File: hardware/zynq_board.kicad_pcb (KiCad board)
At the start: 8 copper layers, 120 x 75 mm, 411 parts, among them J1 USB_OTG, J10 DM3CS, J11 USB_OTG, J12 Conn_01x02, J6 MDR20, J7 LSHM-150-xxx-x-DV-A-S, J9 Conn_01x02, Q1 DMP3056L, U1 xc7z030sbg485, U10 TPS3808G01, U11 MCP1700-2502E_SOT23, U12 MT41K128M8, U13 TPS51206, U14 MT41K128M8, U15 DIFF_OSC, U16 DIFF_OSC, U17 SI53340, U18 NX5P3090, U19 SMP1255PUTG, U2 SFPP_CONN, U20 USB3320, U21 OSC, U22 TLK10031, U23 SN74AXC8T245, U24 SN74AXC8T245, U25 SN74AXC8T245, U26 LSF0102, U27 LSF0102, U28 SN74LVC2T45, U29 SN74LVC2T45, U3 TPS8208x, U30 SN74LVC2T45, U31 SN74LVC2T45, U32 DMF05LCFLP, U33 DMF05LCFLP, U34 TC1262-33, U35 MAX14854, U36 CAT24C02TDI-GT3, U37 EMIF06-MSD02N16, U38 33.333MHZ, U39 SMP1255PUTG, U4 TPS8208x, U40 FT234XD, U41 SN74LV1T126, U42 SN74LV1T126, U5 TPSM84424, U6 TPSM84424, U7 TPS8208x, U8 TPS8208x, U9 TPS8208x

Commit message: Added Power/Protection Circuit
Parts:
- removed C134: 100 nF, Capacitors_SMD:C_0201
- removed C135: 0.1µF, Capacitors_SMD:C_0402
- removed F1: Fuse, Resistors_SMD:R_0402
- removed the REF** at (160.0, 64.0)
- removed the REF** at (74.0, 64.0)
- added C748: 100 nF, Capacitors_SMD:C_0201, B.Cu at (180.0, 116.4)
- added C749: 100 nF, Capacitors_SMD:C_0201, F.Cu at (157.6, 123.8)
- added D2201: P0220SCMCLRP, footprints:DO-214AA, F.Cu at (174.5, 71.5)
- added D2204: BAT54GWJ, Diodes_SMD:D_SOD-123, B.Cu at (175.0, 65.5)
- added F2201: Fuse, Fuse_Holders_and_Fuses:Fuse_SMD1206_Reflow, B.Cu at (175.0, 74.0)
- added T2201: 500 Ohm@100 MHz, footprints:DLW5BTM_5.00x5.00mm, F.Cu at (168.6, 71.5)
- D2202: renamed from D6; moved to B.Cu
- D2203: renamed from D7; moved to B.Cu
- moved D2202 200.9 mm to (175.0, 69.5)
- moved D2203 77.1 mm to (167.7, 70.2), turned to 270 degrees
- moved Q2201 67.2 mm to (162.0, 73.8)
- moved REF** 26.0 mm to (74.0, 64.0)
- moved J1601 10.3 mm to (130.2, 129.2)
- moved C711 7.69 mm to (176.0, 100.7)
- moved C708 7.62 mm to (180.8, 93.2)
- moved C746 7.62 mm to (172.8, 116.4)
- moved C756 7.62 mm to (179.8, 94.7)
- moved C761 7.62 mm to (150.8, 107.2)
- moved C705 7.62 mm to (182.4, 93.2)
- moved C716 7.62 mm to (176.0, 93.2)
- moved C718 7.62 mm to (173.2, 100.9)
- moved C721 7.62 mm to (174.4, 93.2)
- moved C724 7.62 mm to (170.7, 101.4)
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- renumbered C153 to C1001, C154 to C1002, C155 to C1003, C156 to C1004, C157 to C1201, C158 to C1202, C159 to C1203, C160 to C1204, C161 to C1205, C162 to C1206, C163 to C1207, C164 to C1208, C165 to C1209, C166 to C1210, C167 to C1211, C168 to C1212, C169 to C1213, C170 to C1214, C171 to C1215, C172 to C1216, C173 to C1217, C174 to C1218, C175 to C1219, C176 to C1220, C177 to C1221, C178 to C1222, C179 to C1223, C180 to C1224, C181 to C1225, C182 to C1226, C183 to C1227, C184 to C1228, C185 to C1229, C186 to C1230, C187 to C1231, C188 to C1232, C189 to C1233, C190 to C1234, C191 to C1235, C192 to C1236, C193 to C1237, C194 to C1238, C195 to C1301, C196 to C1302, C197 to C1303, C198 to C1304, C199 to C1305, C200 to C1306, C201 to C1307, C202 to C1308, C203 to C1309, C204 to C1310, C205 to C1311, C206 to C1312, C207 to C1313, C208 to C1314, C209 to C1315, C210 to C1316, C211 to C1317, C212 to C1318, C213 to C1319, C214 to C1320, C215 to C1401, C216 to C1402, C217 to C1403, C218 to C1404, C219 to C1405, C220 to C1406, C221 to C1407, C222 to C1408, C231 to C1509, C232 to C1510, C239 to C1801, C240 to C1802, C241 to C1803, C243 to C1901, C244 to C1902, C245 to C1903, C246 to C1904, C247 to C1905, C248 to C1906, C249 to C1907, C250 to C1908, C251 to C1909, C1 to C201, C3 to C203, C4 to C204, C5 to C205, C6 to C206, C7 to C207, C8 to C208, C9 to C209, C10 to C210, C11 to C211, C12 to C212, C13 to C213, C14 to C214, C15 to C215, C16 to C216, C17 to C217, C18 to C218, C19 to C219, C20 to C220, C21 to C221, C22 to C222, C23 to C223, C24 to C224, C25 to C225, C26 to C226, C27 to C227, C28 to C228, C29 to C229, C30 to C230, C31 to C231, C32 to C232, C33 to C233, C34 to C234, C35 to C235, C36 to C236, C37 to C237, C38 to C238, C39 to C239, C40 to C240, C41 to C241, C42 to C242, C43 to C243, C44 to C244, C45 to C245, C46 to C246, C47 to C247, C48 to C248, C49 to C249, C50 to C250, C51 to C251, C52 to C252, C53 to C253, C54 to C254, C55 to C255, C56 to C256, C57 to C257, C58 to C258, C59 to C501, C60 to C502, C61 to C503, C62 to C504, C63 to C505, C64 to C506, C85 to C621, C86 to C622, C87 to C701, C88 to C702, C89 to C703, C90 to C704, C91 to C705, C92 to C706, C93 to C707, C94 to C708, C95 to C709, C96 to C710, C97 to C711, C98 to C712, C99 to C713, C100 to C714, C101 to C715, C102 to C716, C103 to C717, C104 to C718, C105 to C719, C106 to C720, C107 to C721, C108 to C722, C109 to C723, C110 to C724, C111 to C725, C112 to C726, C113 to C727, C114 to C728, C115 to C729, C116 to C730, C117 to C731, C118 to C732, C119 to C733, C120 to C734, C121 to C735, C122 to C736, C123 to C737, C124 to C738, C125 to C739, C126 to C740, C127 to C741, C128 to C742, C129 to C743, C130 to C744, C131 to C745, C132 to C746, C133 to C747, C136 to C750, C137 to C751, C252 to C752, C253 to C753, C254 to C754, C255 to C755, C138 to C756, C256 to C757, C257 to C758, C258 to C759, C259 to C760, C139 to C761, C140 to C762, C141 to C801, C142 to C802, C143 to C803, C144 to C804, C145 to C805, C146 to C901, C147 to C902, C148 to C903, C149 to C904, C150 to C905, C151 to C906, C152 to C907, D1 to D1401, D2 to D1402, D4 to D1701, J6 to J1501, J7 to J1601, J9 to J1702, J10 to J1801, J11 to J1901, J12 to J2201, J1 to J901, L5 to L1901, L1 to L201, Q1 to Q2201, R78 to R1101, R79 to R1102, R80 to R1201, R81 to R1202, R82 to R1203, R83 to R1204, R84 to R1205, R85 to R1206, R86 to R1301, R87 to R1302, R88 to R1303, R89 to R1304, R90 to R1305, R91 to R1306, R92 to R1307, R93 to R1308, R94 to R1309, R95 to R1310, R96 to R1311, R97 to R1312, R98 to R1313, R99 to R1314, R100 to R1315, R101 to R1316, R102 to R1317, R103 to R1318, R104 to R1319, R105 to R1320, R106 to R1401, R107 to R1402, R108 to R1403, R109 to R1404, R110 to R1405, R111 to R1406, R112 to R1407, R113 to R1408, R114 to R1409, R115 to R1410, R116 to R1411, R117 to R1412, R118 to R1413, R119 to R1414, R120 to R1415, R121 to R1416, R122 to R1417, R123 to R1418, R124 to R1419, R125 to R1420, R126 to R1421, R142 to R1701, R143 to R1702, R144 to R1801, R145 to R1802, R146 to R1803, R147 to R1804, R148 to R1805, R149 to R1806, R150 to R1807, R151 to R1808, R152 to R1809, R153 to R1810, R154 to R1811, R155 to R1812, R156 to R1813, R157 to R1814, R158 to R1815, R159 to R1816, R161 to R1901, R162 to R1902, R163 to R1903, R164 to R1904, R165 to R1905, R1 to R501, R2 to R502, R3 to R503, R4 to R504, R5 to R505, R6 to R506, R7 to R507, R8 to R508, R9 to R509, R10 to R510, R11 to R511, R39 to R701, R40 to R702, R41 to R703, R42 to R704, R43 to R705, R44 to R706, R45 to R707, R46 to R708, R47 to R709, R48 to R710, R49 to R711, R50 to R712, R51 to R713, R166 to R714, R53 to R715, R52 to R716, R54 to R717, R55 to R718, R56 to R719, R57 to R720, R58 to R721, R59 to R722, R60 to R723, R61 to R724, R62 to R725, R63 to R726, R64 to R727, R65 to R728, R167 to R729, R168 to R730, R66 to R731, R67 to R732, R68 to R801, R69 to R802, R70 to R803, R71 to R804, R72 to R901, R73 to R902, R74 to R903, R75 to R904, R76 to R905, U22 to U1201, U23 to U1401, U24 to U1402, U25 to U1403, U26 to U1404, U27 to U1405, U28 to U1501, U29 to U1502, U30 to U1503, U31 to U1504, U32 to U1505, U33 to U1506, U34 to U1507, U35 to U1508, U36 to U1801, U37 to U1802, U38 to U1803, U39 to U1901, U40 to U1902, U41 to U1903, U42 to U1904, U1 to U201, U2 to U501, U3 to U601, U4 to U602, U5 to U603, U6 to U604, U7 to U605, U8 to U606, U9 to U607, U10 to U608, U11 to U609, U12 to U701, U13 to U702, U14 to U703, U15 to U801, U16 to U802, U17 to U803, U18 to U901, U19 to U902, U20 to U903, U21 to U904
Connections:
- D2202 pad 2: Net-(D6-Pad2) -> Net-(D2202-Pad2)
- D2203 pad 3: Net-(D6-Pad2) -> Net-(D2203-Pad3)
- U701 pad E3: /DDR/DQ6 -> /DDR/DQ5
- U701 pad F2: /DDR/DQ7 -> /DDR/DQ6
- U701 pad G2: /DDR/DQ5 -> /DDR/DQ7
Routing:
- net Net-(D2202-Pad1): track 0.00 -> 27.0 mm, vias 0 -> 9
- net /DDR/DQ10: track 37.7 -> 17.2 mm
- net /DDR/DQ12: track 41.7 -> 22.0 mm
- net /DDR/DQ11: track 37.4 -> 18.7 mm
- net /DDR/DQ13: track 40.6 -> 22.5 mm
- net GND: track 144.7 -> 162.7 mm, vias 175 -> 184
- net /DDR/DQ14: track 38.9 -> 24.1 mm
- net /DDR/DQ15: track 38.5 -> 25.1 mm
- net /DDR/DDR_DQS1_P: track 39.8 -> 26.9 mm
- net /DDR/DDR_DQS1_N: track 39.1 -> 26.3 mm
- net /DDR/DQ9: track 40.7 -> 31.3 mm
- net Net-(D2201-Pad1): track 0.00 -> 7.22 mm, vias 0 -> 5
- net /DDR/DQ8: track 40.7 -> 33.9 mm
- net /DDR/DDR_DM1: track 40.6 -> 44.8 mm
- net Net-(D2202-Pad2): track 0.00 -> 4.00 mm
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- added copper zone on B.Cu, net Net-(D2201-Pad1)
- added copper zone on F.Cu, net Net-(D2201-Pad1)
- added copper zone on F.Cu, net Net-(D2201-Pad2)
- added copper zone on B.Cu, net Net-(D2202-Pad1)
- added copper zone on F.Cu, net Net-(D2202-Pad1)
- added copper zone on B.Cu, net Net-(F2201-Pad2)

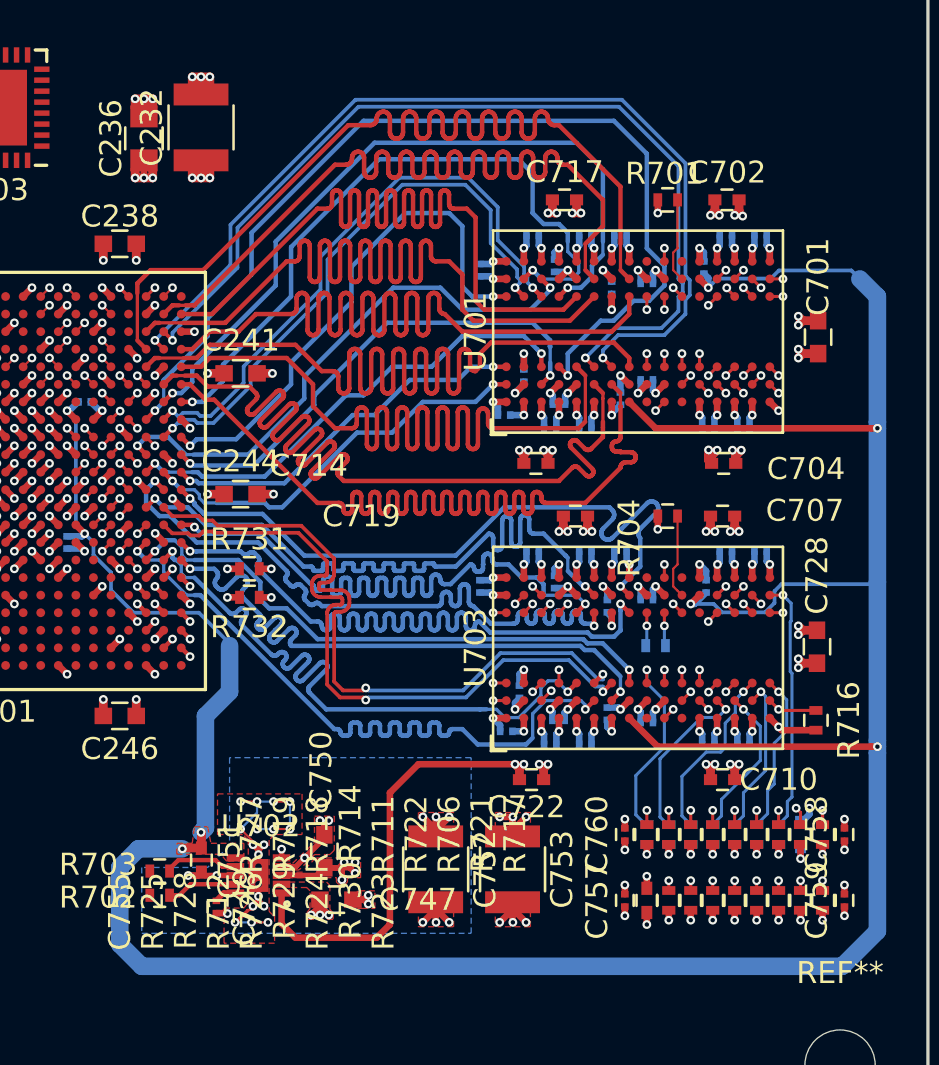
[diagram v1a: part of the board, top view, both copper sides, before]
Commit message: Length matched DDR3 Memory again.
Forgot to keep enough space between the traces and between the meander waves.

Also, I switched to Kicad 5.0 RC2.

Swaped a few ddr signals.
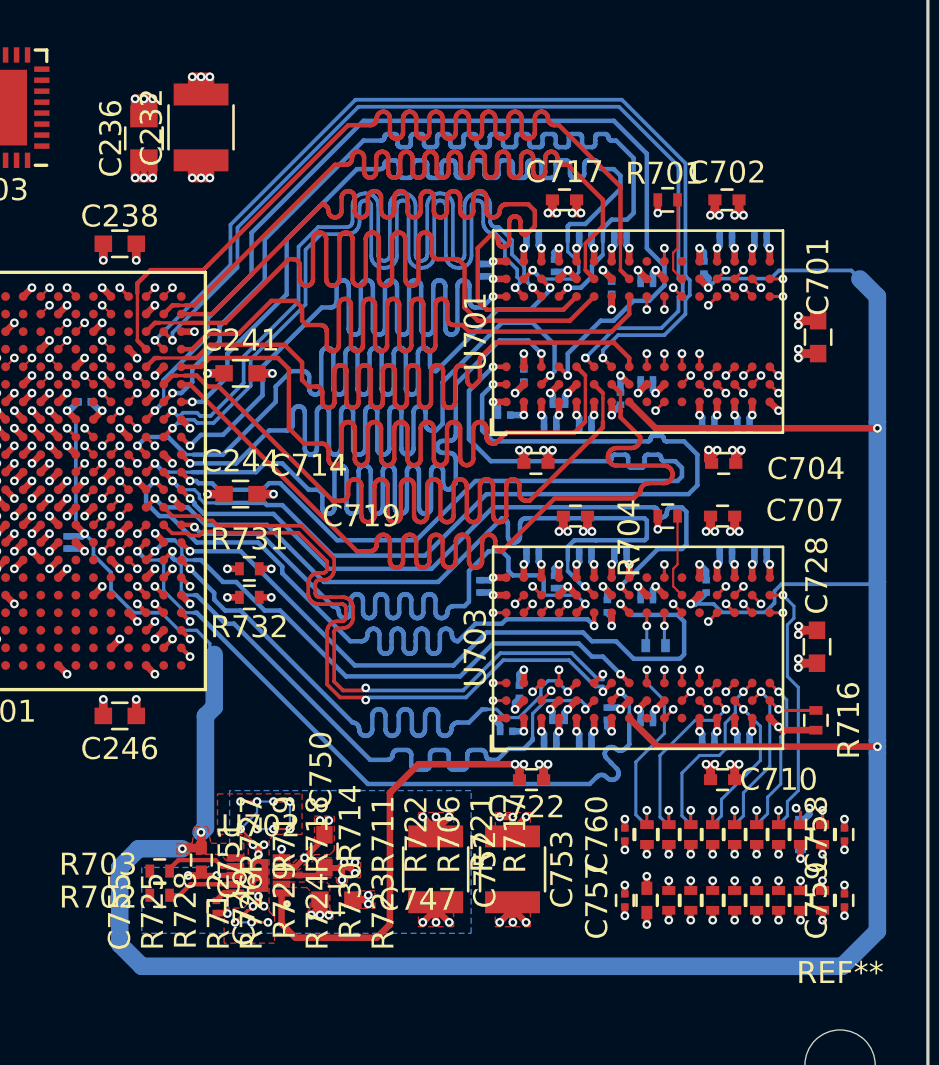
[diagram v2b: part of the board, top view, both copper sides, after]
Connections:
- R1701 pad 1: (no net) -> Net-(R1701-Pad1)
- U1201 pad A10: (no net) -> Net-(U1201-PadA10)
- U1201 pad A9: (no net) -> Net-(U1201-PadA9)
- U1201 pad B8: (no net) -> Net-(J1303-Pad3)
- U1201 pad C11: (no net) -> Net-(U1201-PadC11)
- U1201 pad C8: (no net) -> Net-(J1303-Pad1)
- U1201 pad D4: (no net) -> Net-(U1201-PadD4)
- U1201 pad D6: (no net) -> Net-(J1303-Pad2)
- U1201 pad E5: (no net) -> Net-(J1303-Pad5)
- U1201 pad E9: (no net) -> Net-(J1301-Pad1)
- U1201 pad G12: (no net) -> Net-(U1201-PadG12)
- U1201 pad H12: (no net) -> Net-(U1201-PadH12)
- U1201 pad H9: (no net) -> Net-(U1201-PadH9)
- U1201 pad J9: (no net) -> Net-(J1302-Pad1)
- U1201 pad K12: (no net) -> Net-(U1201-PadK12)
- U1201 pad K8: (no net) -> Net-(U1201-PadK8)
- U1201 pad L12: (no net) -> Net-(U1201-PadL12)
- U1402 pad 10: (no net) -> Net-(U1402-Pad10)
- U1402 pad 14: (no net) -> Net-(U1402-Pad14)
- U1403 pad 10: (no net) -> Net-(U1403-Pad10)
- U1403 pad 14: (no net) -> Net-(U1403-Pad14)
- U1403 pad 15: (no net) -> Net-(U1403-Pad15)
- U1403 pad 9: (no net) -> Net-(U1403-Pad9)
- U1501 pad B2: (no net) -> Net-(R1508-Pad1)
- U1501 pad C2: (no net) -> Net-(R1509-Pad2)
- U1501 pad D2: (no net) -> Net-(R1501-Pad1)
- U1502 pad B2: (no net) -> Net-(R1510-Pad1)
- U1502 pad C2: (no net) -> Net-(R1511-Pad2)
- U1502 pad D2: (no net) -> Net-(R1503-Pad1)
- U1503 pad B2: (no net) -> Net-(R1512-Pad1)
- U1503 pad C2: (no net) -> Net-(R1513-Pad2)
- U1503 pad D2: (no net) -> Net-(R1505-Pad1)
- U1504 pad A2: (no net) -> Net-(U1504-PadA2)
- U1504 pad B2: (no net) -> Net-(R1514-Pad1)
- U1504 pad C2: (no net) -> Net-(R1515-Pad2)
- U1504 pad D2: (no net) -> Net-(10k1501-Pad1)
- U1505 pad 6: (no net) -> Net-(U1505-Pad6)
- U1506 pad 6: (no net) -> Net-(U1506-Pad6)
- U1508 pad 16: (no net) -> Net-(C1513-Pad1)
- U1802 pad 2: (no net) -> Net-(U1802-Pad2)
- U1902 pad 11: (no net) -> Net-(U1902-Pad11)
- U1902 pad 6: (no net) -> Net-(U1902-Pad6)
- U1902 pad 8: (no net) -> Net-(U1902-Pad8)
- U201 pad A10: (no net) -> Net-(U201-PadA10)
- U201 pad A15: (no net) -> Net-(U201-PadA15)
- U201 pad A17: (no net) -> Net-(U201-PadA17)
- U201 pad A22: (no net) -> Net-(U201-PadA22)
- U201 pad B13: (no net) -> Net-(U201-PadB13)
- U201 pad B16: (no net) -> Net-(U201-PadB16)
- U201 pad B17: (no net) -> Net-(U201-PadB17)
- U201 pad B19: (no net) -> Net-(U201-PadB19)
- U201 pad C11: (no net) -> Net-(U201-PadC11)
- U201 pad C13: (no net) -> Net-(U201-PadC13)
- U201 pad C14: (no net) -> /Processing System IO/PS_RESET
- U201 pad C18: (no net) -> Net-(U201-PadC18)
- U201 pad C19: (no net) -> Net-(U201-PadC19)
- U201 pad C4: (no net) -> /GPIO_5
- U201 pad C5: (no net) -> /GPIO_4
- U201 pad C6: (no net) -> /GPIO_3
- U201 pad C8: (no net) -> /GPIO_0
- U201 pad C9: (no net) -> Net-(U201-PadC9)
- U201 pad D10: (no net) -> Net-(U201-PadD10)
- U201 pad D12: (no net) -> Net-(U201-PadD12)
- U201 pad D13: (no net) -> Net-(U201-PadD13)
- U201 pad D16: (no net) -> Net-(U201-PadD16)
- U201 pad D17: (no net) -> Net-(U201-PadD17)
- U201 pad D7: (no net) -> /GPIO_2
- U201 pad D8: (no net) -> /GPIO_1
- U201 pad E14: (no net) -> Net-(U201-PadE14)
- U201 pad E17: (no net) -> Net-(U201-PadE17)
- U201 pad E4: (no net) -> /GPIO_7
- U201 pad E5: (no net) -> /GPIO_6
- U201 pad F11: (no net) -> Net-(U201-PadF11)
- U201 pad F12: (no net) -> Net-(U201-PadF12)
- U201 pad F15: (no net) -> Net-(U201-PadF15)
- U201 pad F5: (no net) -> Net-(U201-PadF5)
- U201 pad F6: (no net) -> Net-(U201-PadF6)
- U201 pad F7: (no net) -> Net-(U201-PadF7)
- U201 pad G16: (no net) -> Net-(U201-PadG16)
- U201 pad G17: (no net) -> Net-(U201-PadG17)
- U201 pad G4: (no net) -> /GPIO_8
- U201 pad G6: (no net) -> Net-(U201-PadG6)
- U201 pad G7: (no net) -> Net-(U201-PadG7)
- U201 pad G8: (no net) -> Net-(U201-PadG8)
- U201 pad G9: (no net) -> Net-(J1101-Pad3)
- U201 pad H10: (no net) -> Net-(J1101-Pad4)
- U201 pad H11: (no net) -> Net-(J1101-Pad1)
- U201 pad H3: (no net) -> Net-(U201-PadH3)
- U201 pad H5: (no net) -> Net-(U201-PadH5)
- U201 pad H6: (no net) -> Net-(U201-PadH6)
- U201 pad H8: (no net) -> Net-(U201-PadH8)
- U201 pad H9: (no net) -> Net-(J1101-Pad2)
- U201 pad J6: (no net) -> Net-(U201-PadJ6)
- U201 pad J7: (no net) -> Net-(U201-PadJ7)
- U201 pad J8: (no net) -> Net-(U201-PadJ8)
- U201 pad K4: (no net) -> /GPIO_9
- U201 pad K7: (no net) -> Net-(U201-PadK7)
- U201 pad K8: (no net) -> Net-(U201-PadK8)
- U201 pad L4: (no net) -> /GPIO_10
- U201 pad L6: (no net) -> Net-(U201-PadL6)
- U201 pad L7: (no net) -> Net-(U201-PadL7)
- U201 pad M4: (no net) -> /GPIO_11
- U201 pad M6: (no net) -> Net-(U201-PadM6)
- U201 pad M7: (no net) -> Net-(U201-PadM7)
- U201 pad M8: (no net) -> Net-(U201-PadM8)
- U201 pad N4: (no net) -> /GPIO_12
- U201 pad N5: (no net) -> Net-(U201-PadN5)
- U201 pad N6: (no net) -> Net-(U201-PadN6)
- U201 pad N8: (no net) -> Net-(U201-PadN8)
- U201 pad P5: (no net) -> Net-(U201-PadP5)
- U201 pad P6: (no net) -> Net-(U201-PadP6)
- U201 pad P7: (no net) -> Net-(U201-PadP7)
- U201 pad P8: (no net) -> Net-(U201-PadP8)
- U201 pad R17: (no net) -> Net-(U201-PadR17)
- U201 pad R3: (no net) -> /GPIO_14
- U201 pad R4: (no net) -> /GPIO_13
- U201 pad R5: (no net) -> Net-(U201-PadR5)
- U201 pad R7: (no net) -> Net-(U201-PadR7)
- U201 pad R8: (no net) -> Net-(U201-PadR8)
- U201 pad T10: (no net) -> Net-(U201-PadT10)
- U201 pad T16: (no net) -> Net-(U201-PadT16)
- U201 pad T17: (no net) -> Net-(U201-PadT17)
- U201 pad U13: (no net) -> Net-(U201-PadU13)
- U201 pad U14: (no net) -> Net-(U201-PadU14)
- U201 pad U16: (no net) -> Net-(U201-PadU16)
- U201 pad U2: (no net) -> /GPIO_15
- U201 pad U7: (no net) -> Net-(R1001-Pad1)
- U201 pad W3: (no net) -> Net-(L202-Pad2)
- U601 pad 7: (no net) -> Net-(R608-Pad2)
- U602 pad 7: (no net) -> Net-(R610-Pad2)
- U603 pad 10: (no net) -> Net-(U603-Pad10)
- U603 pad 15: (no net) -> GND
- U603 pad 16: (no net) -> Net-(U603-Pad16)
- U603 pad 2: (no net) -> Net-(R612-Pad2)
- U603 pad 24: (no net) -> Net-(R605-Pad1)
- U603 pad 4: (no net) -> Net-(U603-Pad4)
- U603 pad 5: (no net) -> Net-(R603-Pad1)
- U603 pad 6: (no net) -> Net-(R601-Pad2)
- U604 pad 15: (no net) -> GND
- U604 pad 16: (no net) -> Net-(U604-Pad16)
- U604 pad 2: (no net) -> Net-(R614-Pad2)
- U604 pad 24: (no net) -> Net-(R606-Pad1)
- U604 pad 4: (no net) -> Net-(U604-Pad4)
- U604 pad 5: (no net) -> Net-(R604-Pad1)
- U604 pad 6: (no net) -> Net-(R602-Pad2)
- U605 pad 7: (no net) -> Net-(R621-Pad2)
- U606 pad 7: (no net) -> Net-(R623-Pad2)
- U607 pad 7: (no net) -> Net-(R625-Pad2)
- U608 pad 1: (no net) -> Net-(C614-Pad1)
- U608 pad 3: (no net) -> Net-(U608-Pad3)
- U701 pad J1: (no net) -> Net-(U701-PadJ1)
- U701 pad J9: (no net) -> Net-(U701-PadJ9)
- U701 pad L1: (no net) -> Net-(U701-PadL1)
- U701 pad L9: (no net) -> Net-(U701-PadL9)
- U701 pad M7: (no net) -> Net-(U701-PadM7)
- U703 pad E3: /DDR/DQ21 -> /DDR/DQ19
- U703 pad F2: /DDR/DQ20 -> /DDR/DQ21
- U703 pad G2: /DDR/DQ19 -> /DDR/DQ20
- U703 pad J1: (no net) -> Net-(U703-PadJ1)
- U703 pad J9: (no net) -> Net-(U703-PadJ9)
- U703 pad L1: (no net) -> Net-(U703-PadL1)
- U703 pad L9: (no net) -> Net-(U703-PadL9)
- U703 pad M7: (no net) -> Net-(U703-PadM7)
- U801 pad 1: (no net) -> Net-(U801-Pad1)
- U801 pad 2: (no net) -> Net-(U801-Pad2)
- U802 pad 1: (no net) -> Net-(U802-Pad1)
- U802 pad 2: (no net) -> Net-(U802-Pad2)
- U803 pad 13: (no net) -> Net-(U803-Pad13)
- U803 pad 14: (no net) -> Net-(U803-Pad14)
- U803 pad 15: (no net) -> Net-(U803-Pad15)
- U803 pad 16: (no net) -> Net-(U803-Pad16)
- U803 pad 8: (no net) -> Net-(U803-Pad8)
- U903 pad 12: (no net) -> Net-(U903-Pad12)
- U903 pad 15: (no net) -> Net-(U903-Pad15)
- U903 pad 16: (no net) -> Net-(U903-Pad16)
- U903 pad 25: (no net) -> Net-(U903-Pad25)
- U903 pad 27: (no net) -> /USB/RESETB
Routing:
- net /DDR/DQ10: track 17.2 -> 41.8 mm
- net /DDR/DQ12: track 22.0 -> 45.9 mm
- net /DDR/DQ11: track 18.7 -> 42.1 mm
- net /DDR/DQ13: track 22.5 -> 44.7 mm
- net /DDR/DQ14: track 24.1 -> 43.0 mm
- net /DDR/DQ15: track 25.1 -> 42.7 mm
- net /DDR/DDR_DQS1_P: track 26.9 -> 44.0 mm
- net /DDR/DDR_DQS1_N: track 26.3 -> 43.5 mm
- net /DDR/DQ9: track 31.3 -> 44.8 mm
- net /DDR/DQ8: track 33.9 -> 44.8 mm
- net /DDR/DQ24: track 24.3 -> 28.6 mm
- net /DDR/DDR_DQS3_P: track 26.5 -> 30.9 mm
- net /DDR/DQ27: track 28.4 -> 32.7 mm
- net /DDR/DQ26: track 25.5 -> 29.8 mm
- net /DDR/DQ25: track 28.4 -> 32.7 mm
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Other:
- board text added: "DQS0 is routed on an outer Layer, but the other Signals of its Group is on an inner Layer. Check, if this is a problem."

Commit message: Layouted most of the Power Circuit and Triggerbus Levelshifters.
Added Footprint for Tantal Caps. Modified Footprint for MDR20 Connector, SD-Card.

Fixed Symbol and Circuit for Power Supervisor/Delay IC.

Also fixed some smaller things in the schematics.
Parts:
- added C1501: 100 nF, Capacitor_SMD:C_0201_0603Metric, B.Cu at (90.0, 95.8)
- added C1502: 100 nF, Capacitor_SMD:C_0201_0603Metric, B.Cu at (90.0, 91.8)
- added C1503: 100 nF, Capacitor_SMD:C_0201_0603Metric, B.Cu at (90.0, 87.8)
- added C1504: 100 nF, Capacitor_SMD:C_0201_0603Metric, B.Cu at (90.0, 83.8)
- added C1505: 100 nF, Capacitor_SMD:C_0201_0603Metric, B.Cu at (88.0, 95.8)
- added C1506: 100 nF, Capacitor_SMD:C_0201_0603Metric, B.Cu at (88.0, 91.8)
- added C1507: 100 nF, Capacitor_SMD:C_0201_0603Metric, B.Cu at (88.0, 87.8)
- added C1508: 100 nF, Capacitor_SMD:C_0201_0603Metric, B.Cu at (88.0, 83.9)
- added C1511: 1 µF 6,3 V, Capacitor_SMD:C_0402_1005Metric, F.Cu at (95.5, 69.5)
- added C1512: 100 nF, Capacitor_SMD:C_0201_0603Metric, F.Cu at (94.5, 69.5)
- added C1513: 1 µF 6,3 V, Capacitor_SMD:C_0402_1005Metric, F.Cu at (85.0, 69.5)
- added C1514: 100 nF, Capacitor_SMD:C_0201_0603Metric, F.Cu at (86.0, 69.5)
- added C1515: 100 nF, Capacitor_SMD:C_0201_0603Metric, F.Cu at (86.0, 77.0)
- added C1516: 1 µF 6,3 V, Capacitor_SMD:C_0402_1005Metric, F.Cu at (85.0, 77.0)
- added C1804: 1nF, Capacitor_SMD:C_0402_1005Metric, F.Cu at (216.1, 98.2)
- added C601: 10uF 25V, Capacitor_SMD:C_1210_3225Metric, F.Cu at (157.0, 65.8)
- added C602: 10uF 25V, Capacitor_SMD:C_1210_3225Metric, F.Cu at (141.0, 65.8)
- added C603: 10uF 25V, Capacitor_SMD:C_1210_3225Metric, F.Cu at (145.0, 65.8)
- added C604: 10uF 25V, Capacitor_SMD:C_1210_3225Metric, F.Cu at (129.0, 65.8)
- added C605: 10uF, Capacitor_SMD:C_0805_2012Metric, F.Cu at (138.5, 76.8)
- added C606: 10uF, Capacitor_SMD:C_0805_2012Metric, F.Cu at (147.0, 76.8)
- added C607: 47uF 6.3V, Capacitor_SMD:C_1210_3225Metric, F.Cu at (134.8, 78.5)
- added C608: 47uF 6.3V, Capacitor_SMD:C_1210_3225Metric, F.Cu at (143.2, 78.5)
- added C609: 47uF 6.3V, Capacitor_SMD:C_1210_3225Metric, F.Cu at (145.0, 72.0)
- added C610: 100uF 6.3V, Capacitor_SMD:C_1210_3225Metric, F.Cu at (141.0, 72.0)
- added C611: 100uF 6.3V, Capacitor_SMD:C_1210_3225Metric, F.Cu at (129.0, 72.0)
- added C612: 220uF 6.3V 15mΩ, footprints:C7343-31_KEMET-D_10.22x5.6mm, B.Cu at (157.0, 67.0)
- added C613: 220uF 6.3V 15mΩ, footprints:C7343-31_KEMET-D_10.22x5.6mm, B.Cu at (141.0, 67.0)
- added C614: 1nF, Capacitor_SMD:C_0402_1005Metric, F.Cu at (126.2, 69.2)
- added C615: 10uF, Capacitor_SMD:C_0805_2012Metric, F.Cu at (129.9, 76.8)
- added C616: 10uF, Capacitor_SMD:C_0805_2012Metric, F.Cu at (121.5, 76.8)
- added C617: 10uF, Capacitor_SMD:C_0805_2012Metric, F.Cu at (155.4, 76.8)
- added C618: 47uF 6.3V, Capacitor_SMD:C_1210_3225Metric, F.Cu at (126.2, 78.5)
- added C619: 47uF 6.3V, Capacitor_SMD:C_1210_3225Metric, F.Cu at (117.7, 78.5)
- added C620: 47uF 6.3V, Capacitor_SMD:C_1210_3225Metric, F.Cu at (151.7, 78.5)
- added D1501: PMEG3020EGWX, Diode_SMD:D_SOD-123, F.Cu at (92.0, 77.0)
- added R1501: 10k, Resistor_SMD:R_0402_1005Metric, B.Cu at (89.9, 90.5)
- added R1502: DNP, Resistor_SMD:R_0402_1005Metric, B.Cu at (88.2, 90.5)
- added R1503: 10k, Resistor_SMD:R_0402_1005Metric, B.Cu at (89.9, 89.5)
- added R1504: DNP, Resistor_SMD:R_0402_1005Metric, B.Cu at (88.2, 89.5)
- added R1505: DNP, Resistor_SMD:R_0402_1005Metric, B.Cu at (89.9, 82.5)
- added R1506: 10k, Resistor_SMD:R_0402_1005Metric, B.Cu at (88.2, 82.5)
- added R1507: DNP, Resistor_SMD:R_0402_1005Metric, B.Cu at (89.9, 81.5)
- added R1508: 270, Resistor_SMD:R_0402_1005Metric, F.Cu at (85.0, 91.5)
- added R1509: 270, Resistor_SMD:R_0402_1005Metric, F.Cu at (85.0, 90.5)
- added R1510: 270, Resistor_SMD:R_0402_1005Metric, F.Cu at (85.0, 89.5)
- added R1511: 270, Resistor_SMD:R_0402_1005Metric, F.Cu at (85.0, 88.5)
- added R1512: 270, Resistor_SMD:R_0402_1005Metric, F.Cu at (85.0, 87.5)
- added R1513: 270, Resistor_SMD:R_0402_1005Metric, F.Cu at (85.0, 86.5)
- added R1514: 270, Resistor_SMD:R_0402_1005Metric, F.Cu at (85.0, 85.5)
- added R1515: 270, Resistor_SMD:R_0402_1005Metric, F.Cu at (85.0, 84.5)
- added R1516: 10k, Resistor_SMD:R_0402_1005Metric, B.Cu at (88.2, 81.5)
- added R1817: 3M, Resistor_SMD:R_0402_1005Metric, F.Cu at (200.2, 102.4)
- added R1818: 560k, Resistor_SMD:R_0402_1005Metric, F.Cu at (210.7, 98.2)
- added R1819: 100k, Resistor_SMD:R_0402_1005Metric, F.Cu at (220.7, 92.1)
- added R601: 31.6k, Resistor_SMD:R_0402_1005Metric, F.Cu at (152.0, 72.4)
- added R602: 31.6k, Resistor_SMD:R_0402_1005Metric, F.Cu at (136.0, 72.4)
- added R603: 31.6k, Resistor_SMD:R_0402_1005Metric, F.Cu at (151.0, 72.4)
- added R604: 3.01k, Resistor_SMD:R_0402_1005Metric, F.Cu at (135.0, 72.4)
- added R605: 40.2k, Resistor_SMD:R_0402_1005Metric, F.Cu at (145.4, 69.0)
- added R606: 124k, Resistor_SMD:R_0402_1005Metric, F.Cu at (129.2, 69.0)
- added R607: 100k, Resistor_SMD:R_0402_1005Metric, F.Cu at (134.9, 82.0)
- added R608: 187k 1%, Resistor_SMD:R_0402_1005Metric, B.Cu at (135.2, 79.5)
- added R609: 150k 1%, Resistor_SMD:R_0402_1005Metric, B.Cu at (135.2, 78.5)
- added R610: 470k 1%, Resistor_SMD:R_0402_1005Metric, B.Cu at (143.8, 79.5)
- added R611: 150k 1%, Resistor_SMD:R_0402_1005Metric, B.Cu at (143.8, 78.5)
- added R612: 10k, Resistor_SMD:R_0402_1005Metric, F.Cu at (148.0, 72.4)
- added R613: 1.37k, Resistor_SMD:R_0402_1005Metric, F.Cu at (149.0, 72.4)
- added R614: 10k, Resistor_SMD:R_0402_1005Metric, F.Cu at (132.0, 72.4)
- added R615: 15k, Resistor_SMD:R_0402_1005Metric, F.Cu at (133.0, 72.4)
- added R616: 100k, Resistor_SMD:R_0402_1005Metric, F.Cu at (137.0, 72.4)
- added R617: 100k, Resistor_SMD:R_0402_1005Metric, F.Cu at (153.0, 72.4)
- added R618: 3M, Resistor_SMD:R_0402_1005Metric, F.Cu at (124.2, 69.2)
- added R619: 270k, Resistor_SMD:R_0402_1005Metric, F.Cu at (125.2, 69.2)
- added R620: 100k, Resistor_SMD:R_0402_1005Metric, F.Cu at (124.1, 81.5)
- added R621: 30k 1%, Resistor_SMD:R_0402_1005Metric, B.Cu at (126.7, 79.5)
- added R622: 120k 1%, Resistor_SMD:R_0402_1005Metric, B.Cu at (126.7, 78.5)
- added R623: 75k 1%, Resistor_SMD:R_0402_1005Metric, B.Cu at (118.2, 79.5)
- added R624: 150k 1%, Resistor_SMD:R_0402_1005Metric, B.Cu at (118.2, 78.5)
- added R625: 68k 1%, Resistor_SMD:R_0402_1005Metric, B.Cu at (152.2, 79.5)
- added R626: 100k 1%, Resistor_SMD:R_0402_1005Metric, B.Cu at (152.2, 78.5)
- added R627: 100k, Resistor_SMD:R_0402_1005Metric, F.Cu at (121.3, 72.0)
- added R628: 43k, Resistor_SMD:R_0402_1005Metric, F.Cu at (123.2, 69.2)
- added SW1801: SW_Push, Button_Switch_SMD:SW_SPST_PTS645, F.Cu at (202.8, 95.0)
- added U1804: TPS3808G01, Package_DFN_QFN:Texas_S-PWSON-N6, F.Cu at (213.0, 93.0)
- C1509, C1510: footprint Capacitors_SMD:C_0402 -> Capacitor_SMD:C_0402_1005Metric
- C201, C203, C234, C239: footprint Capacitors_SMD:C_1210 -> Capacitor_SMD:C_0603_1608Metric
- D2204: value BAT54GWJ -> PMEG3020EGWX
- J1801: moved to F.Cu
- U1505, U1506, U1802: moved to B.Cu
- U608: footprint Housings_DFN_QFN:DFN-6-1EP_2x2mm_Pitch0.65mm -> Package_DFN_QFN:Texas_S-PWSON-N6
- moved C201 307.4 mm to (154.5, 130.5)
- moved L201 281.2 mm to (135.0, 105.0)
- moved C217 259.6 mm to (141.0, 115.5), turned to 180 degrees
- moved C1301 129.3 mm to (-6.40, 149.8)
- moved C1302 129.3 mm to (-17.8, 158.8)
- moved C1303 129.3 mm to (-0.72, 140.9)
- moved C1304 129.3 mm to (-6.40, 145.3)
- moved C1305 129.3 mm to (-12.1, 149.8)
- moved C1306 129.3 mm to (-17.8, 154.3)
- moved C1307 129.3 mm to (-6.40, 140.9)
- moved C1308 129.3 mm to (-12.1, 145.3)
- moved C1309 129.3 mm to (-17.8, 149.8)
- moved C1310 129.3 mm to (-12.1, 140.9)
- moved C1311 129.3 mm to (-12.1, 154.3)
- moved C1312 129.3 mm to (-17.8, 145.3)
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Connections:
- net Net-(C1903-Pad1) renamed /USB-UART/USB_UART_P
- net Net-(C1905-Pad1) renamed /USB-UART/USB_UART_N
- J1501 pad 10: /Triggerbus/B -> /Triggerbus/Z
- J1501 pad 19: /Triggerbus/Y -> /Triggerbus/B
- J1501 pad 20: /Triggerbus/Z -> /Triggerbus/A
- J1501 pad 9: /Triggerbus/A -> /Triggerbus/Y
- U1504 pad A2: Net-(U1504-PadA2) -> VCCO_MIO0
- U1505 pad 1: /Triggerbus/EXT_TRIG_OUT_0 -> Net-(U1505-Pad1)
- U1505 pad 3: /Triggerbus/EXT_TRIG_OUT_1 -> /Triggerbus/EXT_TRIG_OUT_0
- U1505 pad 4: /Triggerbus/EXT_TRIG_OUT_2 -> /Triggerbus/EXT_TRIG_OUT_1
- U1505 pad 5: /Triggerbus/EXT_TRIG_OUT_3 -> /Triggerbus/EXT_TRIG_OUT_2
- U1505 pad 6: Net-(U1505-Pad6) -> /Triggerbus/EXT_TRIG_OUT_3
- U1506 pad 1: /Triggerbus/EXT_TRIG_IN_0 -> /Triggerbus/EXT_TRIG_IN_3
- U1506 pad 3: /Triggerbus/EXT_TRIG_IN_1 -> Net-(U1506-Pad3)
- U1506 pad 4: /Triggerbus/EXT_TRIG_IN_2 -> /Triggerbus/EXT_TRIG_IN_0
- U1506 pad 5: /Triggerbus/EXT_TRIG_IN_3 -> /Triggerbus/EXT_TRIG_IN_1
- U1506 pad 6: Net-(U1506-Pad6) -> /Triggerbus/EXT_TRIG_IN_2
- U1507 pad 4: (no net) -> GND
- U608 pad 1: Net-(C614-Pad1) -> +5V
- U608 pad 2: GND -> Net-(C614-Pad1)
- U608 pad 4: +5V -> Net-(U608-Pad4)
- U608 pad 5: +5V -> GND
- U608 pad 7: (no net) -> GND
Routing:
- net GND: track 162.6 -> 244.6 mm, vias 184 -> 447
- net /PG: track 0.57 -> 56.8 mm
- net /Triggerbus/3.3V_OUT: track 0.00 -> 33.8 mm, vias 0 -> 1
- net /PMIC/EN_3V3: track 0.00 -> 30.3 mm
- net /Triggerbus/5V_OUT: track 0.00 -> 30.3 mm
- net /PMIC/EN_1V0_MGT: track 0.00 -> 26.5 mm, vias 0 -> 3
- net VCCO_34: track 7.92 -> 30.2 mm, vias 14 -> 34
- net /Camera Connector/LVDS_CLK0_N: track 0.00 -> 20.7 mm
- net /Camera Connector/LVDS_CLK0_P: track 0.00 -> 20.6 mm
- net Net-(D2202-Pad1): track 27.0 -> 8.44 mm, vias 9 -> 15
- net /Processing System IO/SDIO0_CD: track 0.00 -> 16.7 mm, vias 0 -> 2
- net /Camera Connector/D0_N: track 0.00 -> 16.4 mm
- net /Camera Connector/D0_P: track 0.00 -> 16.3 mm
- net /PMIC/EN_1V2_MGT: track 0.00 -> 16.0 mm
- net /Camera Connector/D4_P: track 0.00 -> 15.0 mm
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- added copper zone on B.Cu, net +1V0
- added copper zone on F.Cu, net +1V0
- added copper zone on F.Cu, net +1V0_MGT
- added copper zone on F.Cu, net +1V2_MGT
- added copper zone on B.Cu, net +5V
- added copper zone on F.Cu, net +5V
- added copper zone on PWR3.Cu, net +5V
- added copper zone on B.Cu, net /V_IN
- added copper zone on F.Cu, net /V_IN
- added copper zone on GND1.Cu, net Net-(R613-Pad2)
- added copper zone on GND1.Cu, net Net-(R615-Pad2)
- added copper zone on F.Cu, net VCCO_34
- added copper zone on F.Cu, net VCCO_MIO0
- added copper zone on PWR4.Cu, net VCCO_MIO0
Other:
- net class PWR_TRIG added: clearance 0.2, trace_width 0.5, via_dia 0.4, via_drill 0.2
- net class TRIGGER_SIG added: clearance 0.2, trace_width 0.2, via_dia 0.4, via_drill 0.2
